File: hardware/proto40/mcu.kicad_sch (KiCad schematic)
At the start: 19 parts, among them J201 Conn_ARM_SWD_TagConnect_TC2030, J202 UART, SW201 START, U201 STM32C071C8Tx

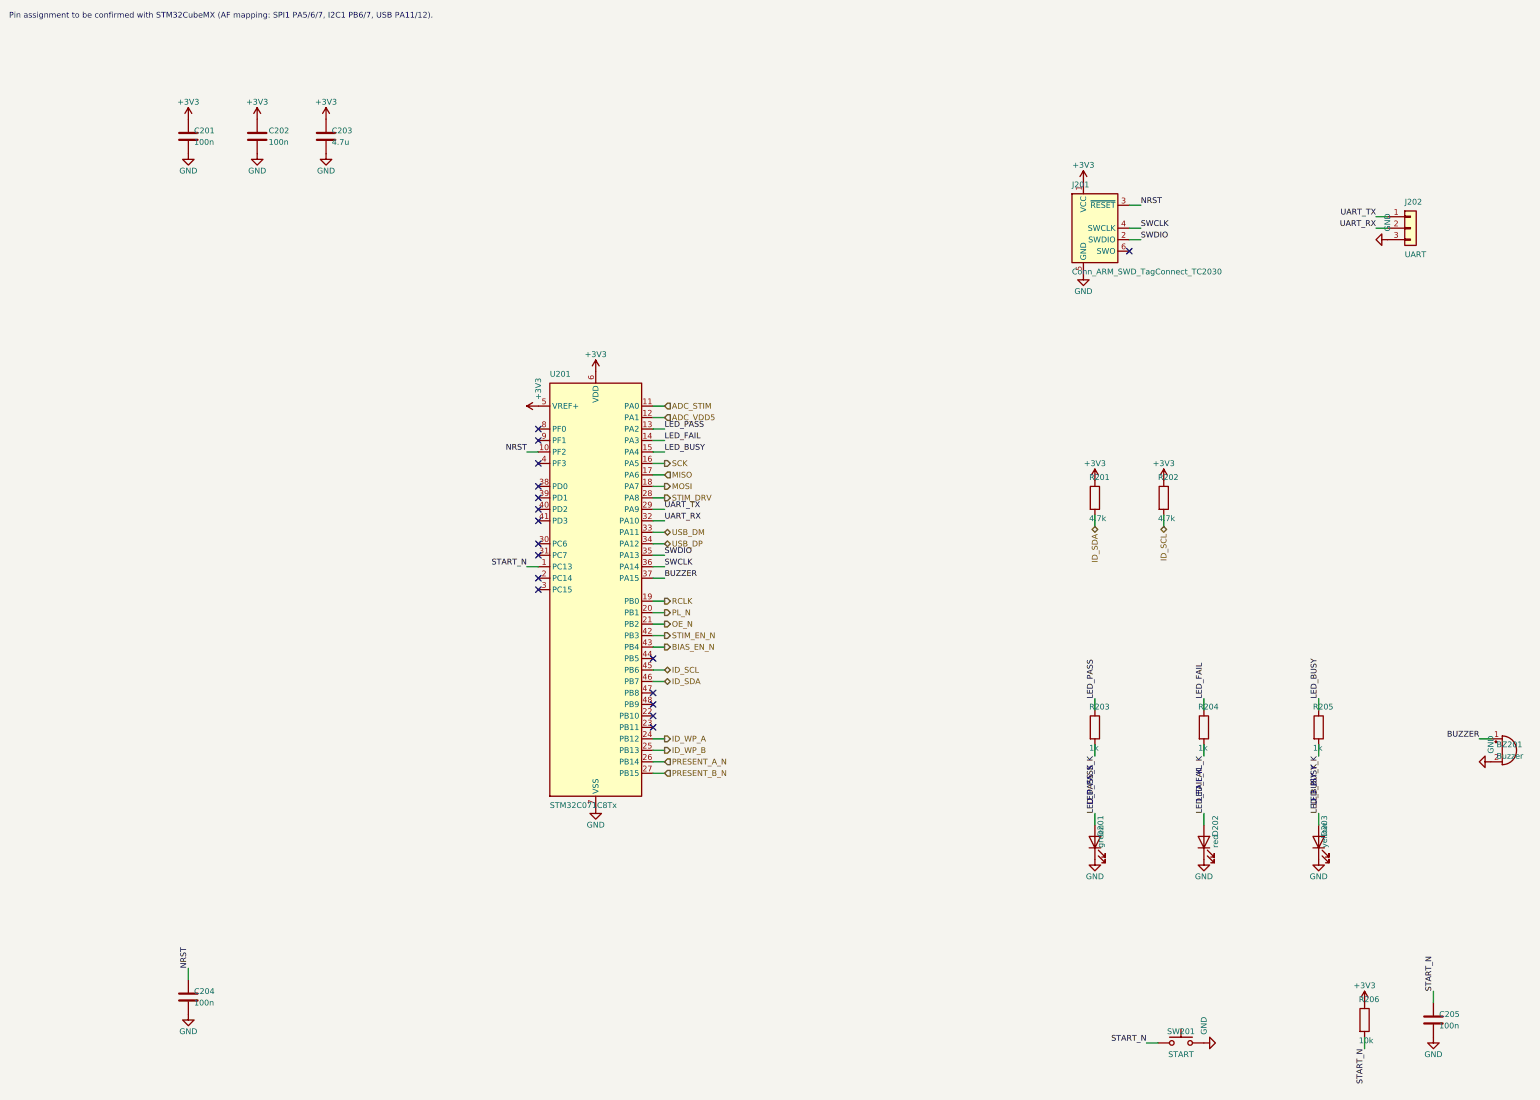
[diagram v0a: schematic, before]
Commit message: Redraw Proto40 schematic with wired functional blocks
Review feedback: text overlapped components and parts were isolated
islands joined only by labels, so connectivity was hard to follow.

- Generator: polyline wires, automatic junctions, text placement from
  the real symbol body graphics, KiCad field-angle handling for rotated
  symbols, power symbols oriented normally on horizontal pins
- Sheets redrawn left-to-right with wired blocks: channel cells, BIAS
  rail, decoupling on IC power pins, pull-ups on their lines, control
  ladder across the six groups, visible 165 chain, wired root hierarchy
  (MCU -> Control -> both sides) and cross-side LOOP
- layoutcheck.py: rejects text/text, text/body, text/wire overlaps and
  wires through bodies; CI runs the generator with --strict
- check_proto40.py: finds parts by sheet path and follows pins, so it no
  longer depends on net names or reference numbering

ERC 0 violations, design-intent audit PASS, layout issues 0.

Co-Authored-By: Claude Opus 5.5 <noreply@anthropic.com>
Claude-Session: https://claude.ai/code/session_01UG7pR5ZtgvoVGRWFojzQKf
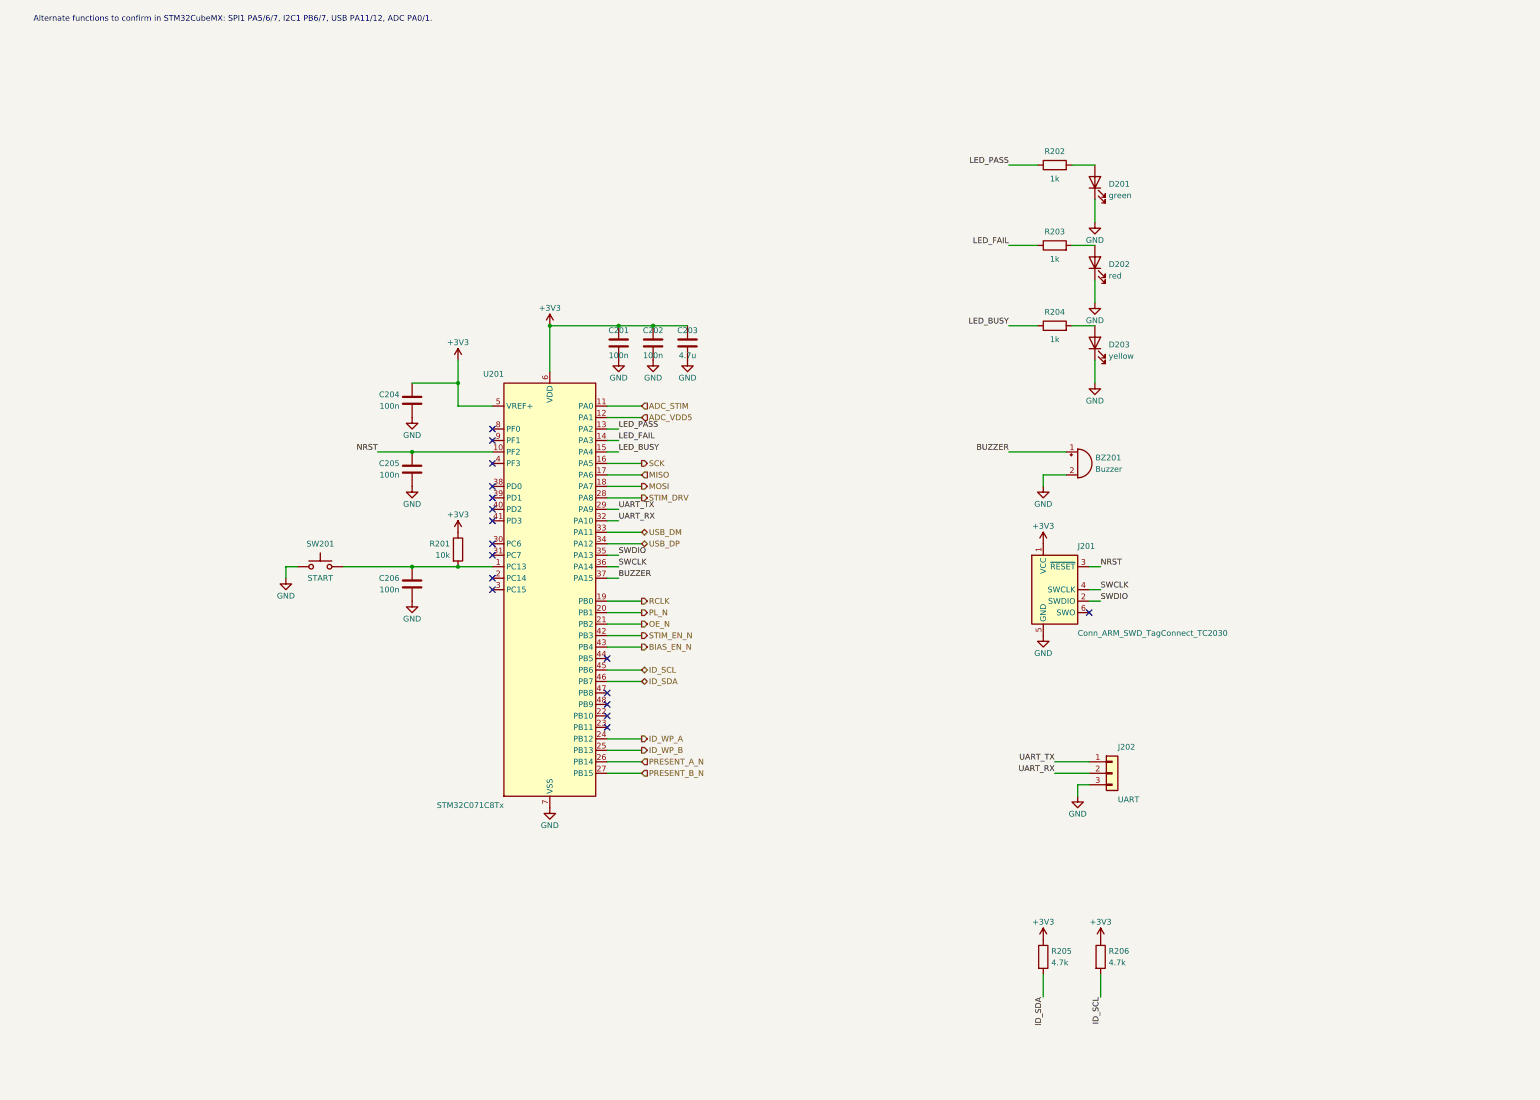
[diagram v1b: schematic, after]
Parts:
- added C206: 100n, Capacitor_SMD:C_0603_1608Metric, symbol Device:C
- BZ201: Note passive piezo, driven by GPIO PWM -> passive piezo, GPIO PWM
- R201: value 4.7k -> 10k
- R202: value 4.7k -> 1k
- R205: value 1k -> 4.7k
- R206: value 10k -> 4.7k
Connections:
- net +3V3: now also C204.1, R205.1; no longer R202.1
- net GND: now also SW201.1, C206.2; no longer SW201.2
- net ID_SCL: now also R206.2; no longer R202.2
- net ID_SDA: now also R205.2; no longer R201.2
- net LED_BUSY: now also R204.1; no longer R205.1
- net LED_FAIL: now also R203.1; no longer R204.1
- net LED_PASS: now also R202.1; no longer R203.1
- net NRST: now also C205.1; no longer C204.1
- net LED_BUSY_K: no longer names the net of D203.2 (A)
- net LED_BUSY_K: now also R204.2; no longer R205.2
- net LED_FAIL_K: no longer names the net of D202.2 (A)
- net LED_FAIL_K: now also R203.2; no longer R204.2
- net LED_PASS_K: no longer names the net of D201.2 (A)
- net LED_PASS_K: now also R202.2; no longer R203.2
- removed net START_N: C205.1, R206.2, SW201.1, U201.1 (PC13)
- new net: C206.1, R201.2, SW201.2, U201.1 (PC13)
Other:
- note added: "Alternate functions to confirm in STM32CubeMX: SPI1 PA5/6/7, I2C1 PB6/7, USB PA11/12, ADC PA0/1."
- note removed: "Pin assignment to be confirmed with STM32CubeMX (AF mapping: SPI1 PA5/6/7, I2C1 PB6/7, USB PA11/12)."
- title: Proto40 – STM32C071 controller, USB, UI, debug -> Proto40 – STM32C071 controller, UI, debug
- moved on the sheet: BZ201, C201, C202, C203, C204, C205, D201, D202, D203, J201, J202, R201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
